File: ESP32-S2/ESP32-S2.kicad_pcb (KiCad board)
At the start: 2 copper layers, 27.9 x 70 mm, 40 parts, among them J1 Conn_01x18_Male, J2 Conn_01x22_Male, J3 USB_A, J4 TYPE-C-31-M-12, Q2 L8050QLT1G, Q3 L8050QLT1G, SW1 SW_Push, SW2 SW_Push, U2 ESP32-S2-WROOM-ESP32-S2-WROOM, U3 AMS1117-3.3, U4 CH340C

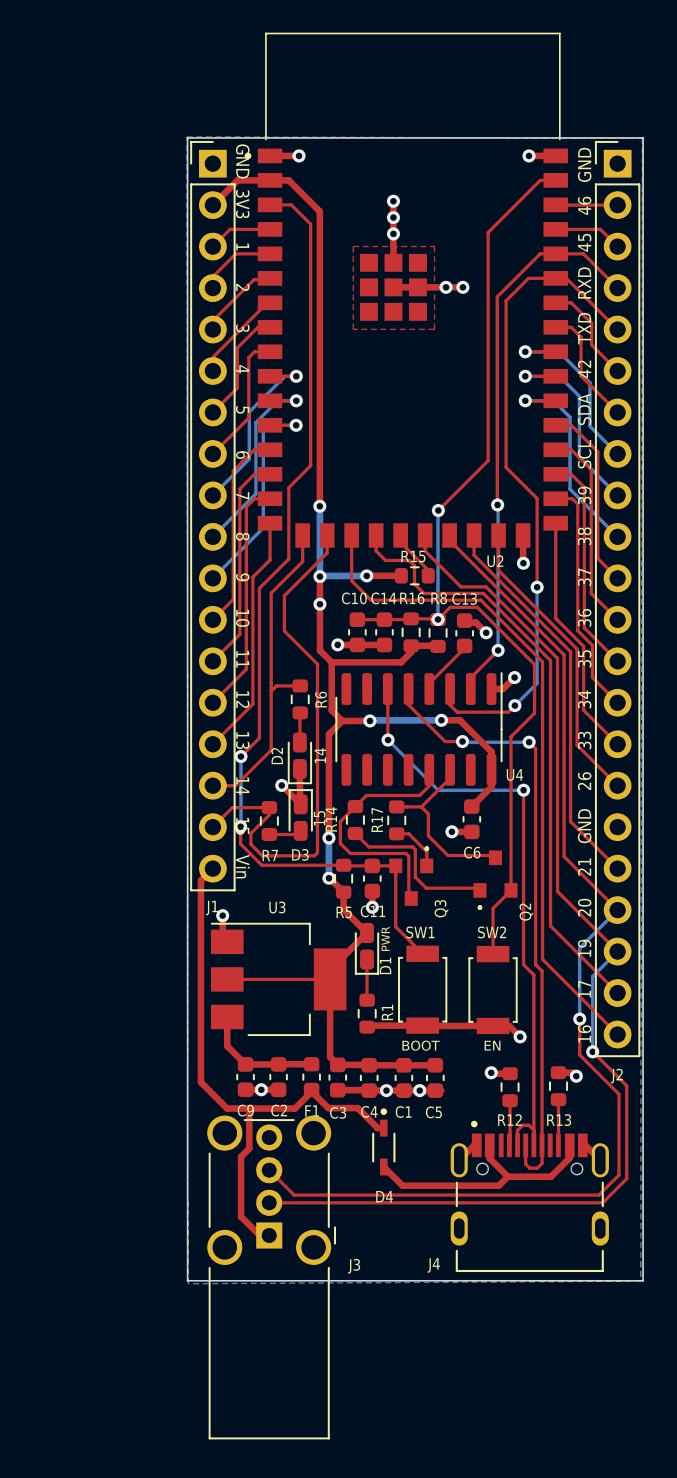
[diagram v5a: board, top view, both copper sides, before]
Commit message: Updated and optimised routing
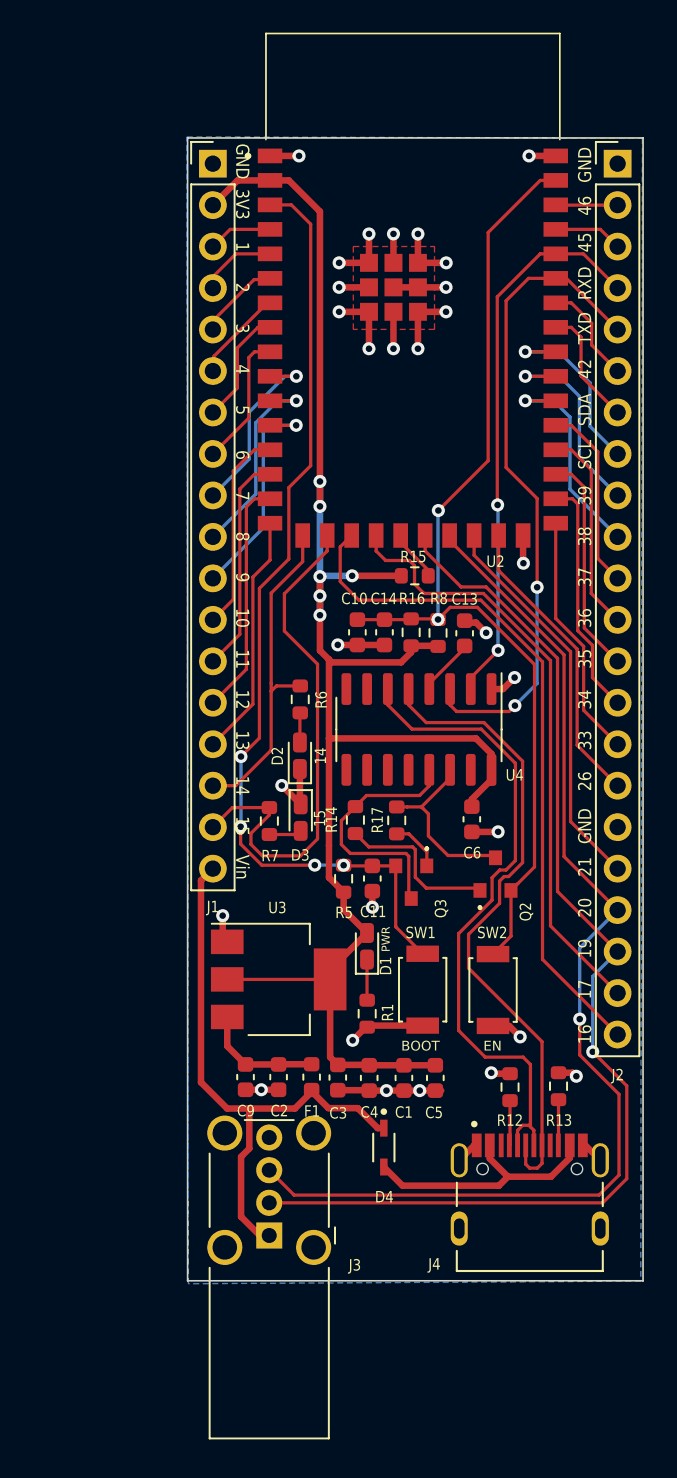
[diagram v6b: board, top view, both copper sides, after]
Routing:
- net GND: track 51.3 -> 64.9 mm, vias 21 -> 29
- net +3V3: track 103.2 -> 106.9 mm, vias 8 -> 6
- net /DN1: track 38.2 -> 40.5 mm, vias 2 -> 0
- net /DP1: track 38.5 -> 40.5 mm, vias 2 -> 0
- net /GPIO16: track 41.3 -> 42.3 mm
- net /GPIO0: vias 2 -> 4

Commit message: added name, corrected annotations
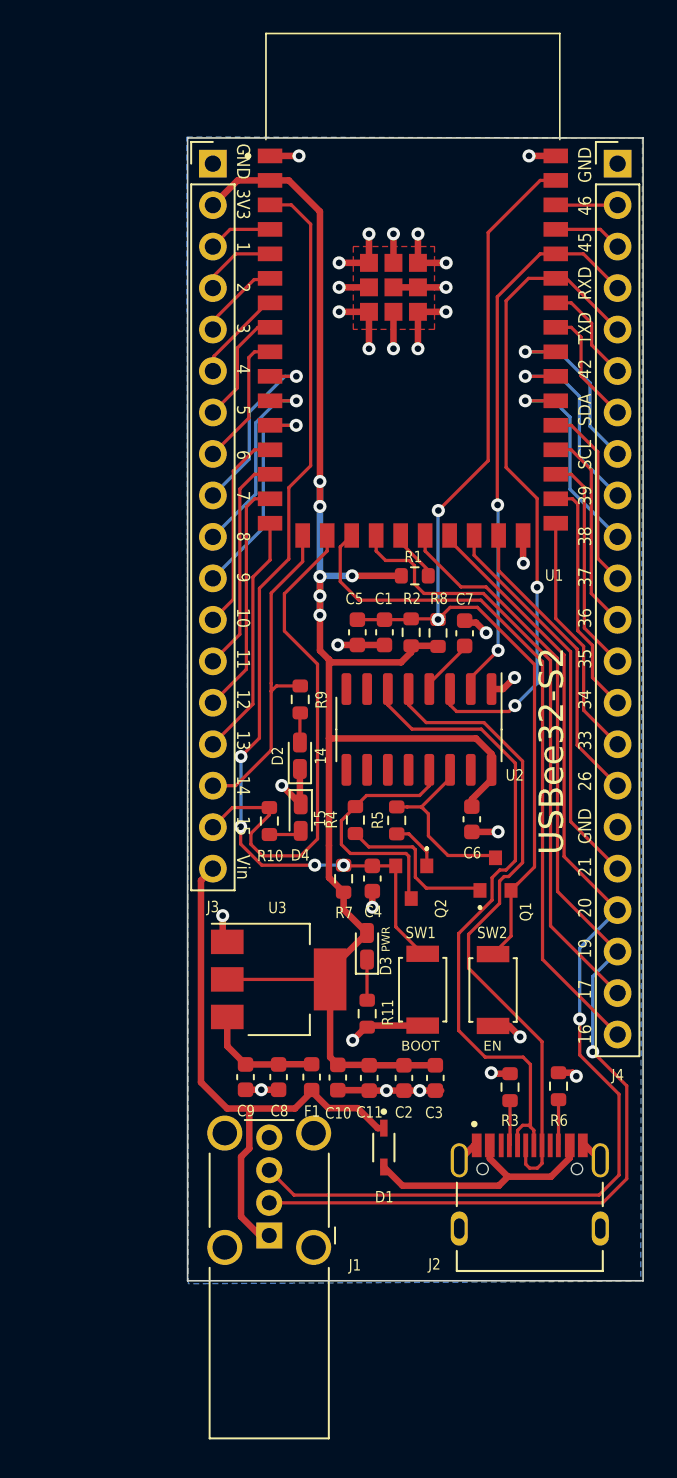
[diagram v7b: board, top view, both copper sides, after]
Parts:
- moved REF** 0.31 mm to (143.8, 71.0)
- moved REF** 0.16 mm to (154.4, 70.8)
- renumbered C14 to C1, C3 to C10, C4 to C11, C1 to C2, C5 to C3, C11 to C4, C10 to C5, C13 to C7, C2 to C8, D4 to D1, D1 to D3, D3 to D4, J3 to J1, J4 to J2, J1 to J3, J2 to J4, Q2 to Q1, Q3 to Q2, R15 to R1, R7 to R10, R1 to R11, R16 to R2, R12 to R3, R14 to R4, R17 to R5, R13 to R6, R5 to R7, R6 to R9, U2 to U1, U4 to U2
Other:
- board text added: "USBee32-S2"
